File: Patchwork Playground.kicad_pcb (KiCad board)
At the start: 2 copper layers, 100 x 60 mm, 87 parts, among them J1 SWD_HEADER, J2 USB_C_Receptacle_USB2.0, J3 PADS, J4 POGO, J5 PADS, J6 JST-GH-4P, SW1 SW_SPDT, SW2 SW_SPDT, SW3 SW_SPDT, SW4 BUTTON, SW5 BUTTON, SW6 SW_SPDT, SW7 SW_SPDT, SW8 SW_SPDT, U1 SMF05CT1G, U2 M3406, U3 BQ21040DBVR, U4 SMF05CT1G, U5 QMC5883L, U6 BC805M, U7 LSM6DSV

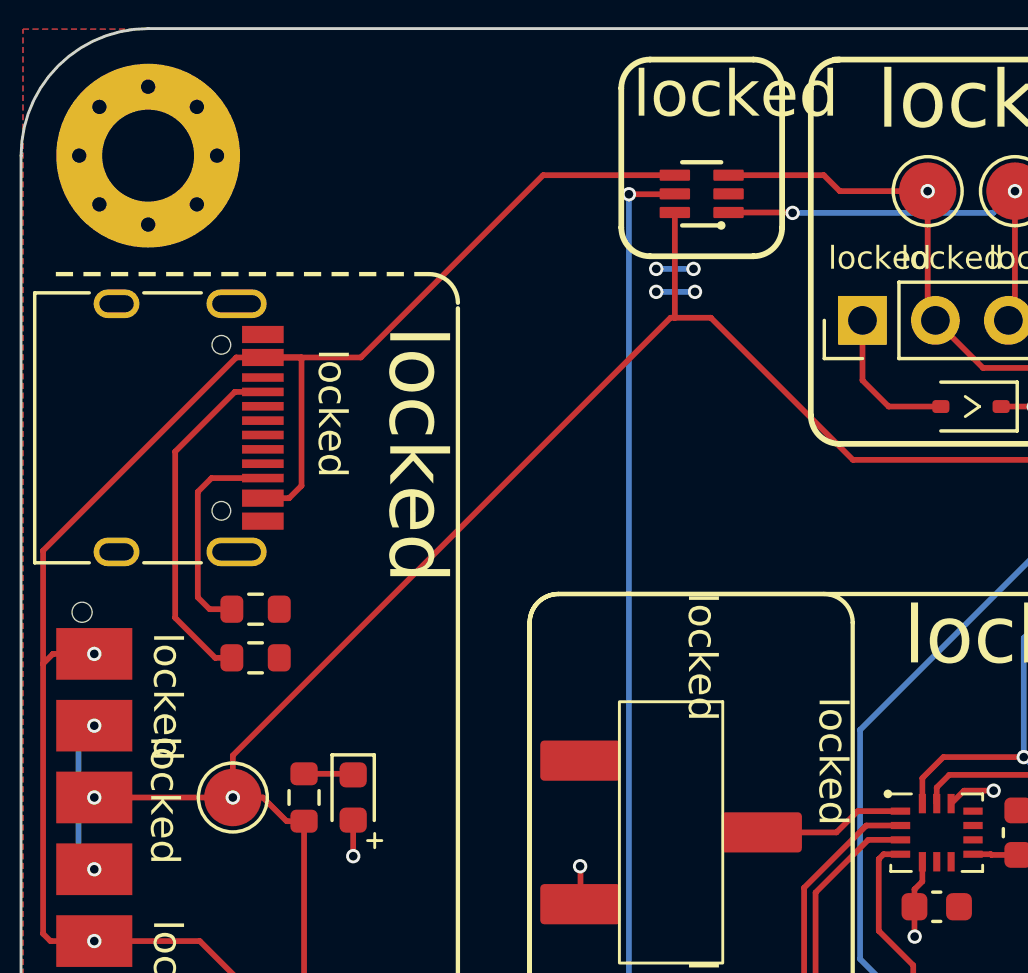
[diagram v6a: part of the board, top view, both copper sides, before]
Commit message: Minor routing changes
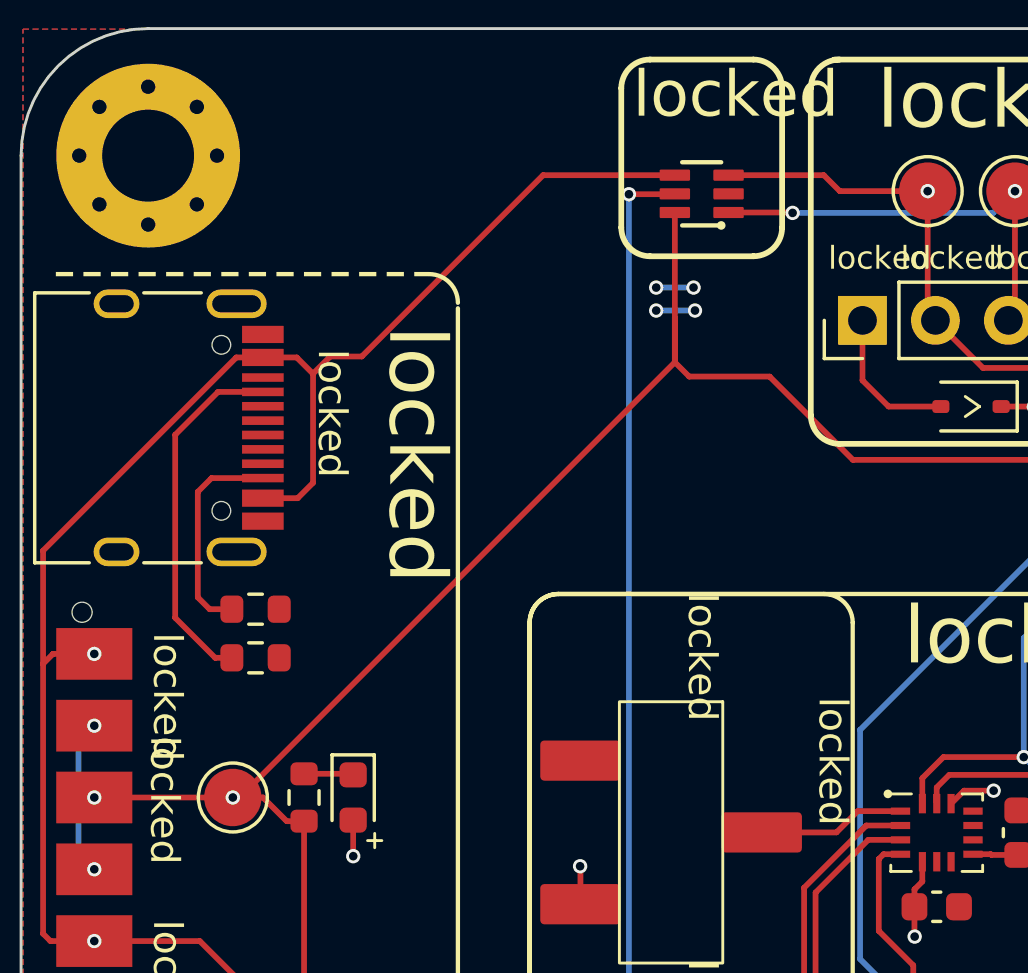
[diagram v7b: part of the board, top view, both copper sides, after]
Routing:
- net +5V: track 94.5 -> 93.4 mm
- net DOCK: track 84.6 -> 85.5 mm
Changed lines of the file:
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@@
   (via (at 100.4831 100.2565) (size 0.5) (drill 0.3) (layers "F.Cu" "B.Cu") (net 2))
   (via (at 114.4 126.1) (size 0.5) (drill 0.3) (layers "F.Cu" "B.Cu") (net 2))
-  (via (at 120.05 80.15) (size 0.5) (drill 0.3) (layers "F.Cu" "B.Cu") (free) (net 2))
-  (via (at 121.35 79.35) (size 0.5) (drill 0.3) (layers "F.Cu" "B.Cu") (free) (net 2))
-  (via (at 120.05 79.35) (size 0.5) (drill 0.3) (layers "F.Cu" "B.Cu") (free) (net 2))
+  (via (at 120.05 80.8) (size 0.5) (drill 0.3) (layers "F.Cu" "B.Cu") (free) (net 2))
+  (via (at 121.35 80) (size 0.5) (drill 0.3) (layers "F.Cu" "B.Cu") (free) (net 2))
+  (via (at 120.05 80) (size 0.5) (drill 0.3) (layers "F.Cu" "B.Cu") (free) (net 2))
   (via (at 100.4831 95.2565) (size 0.5) (drill 0.3) (layers "F.Cu" "B.Cu") (net 2))
-  (via (at 121.4 80.15) (size 0.5) (drill 0.3) (layers "F.Cu" "B.Cu") (free) (net 2))
+  (via (at 121.4 80.8) (size 0.5) (drill 0.3) (layers "F.Cu" "B.Cu") (free) (net 2))
   (segment (start 99.9331 95.8065) (end 100.4831 95.2565) (width 0.2) (layer "B.Cu") (net 2))
   (segment (start 100.4831 100.2565) (end 99.9331 99.7065) (width 0.2) (layer "B.Cu") (net 2))
-  (segment (start 121.35 79.35) (end 120.05 79.35) (width 0.2) (layer "B.Cu") (net 2))
-  (segment (start 120.05 80.15) (end 121.4 80.15) (width 0.2) (layer "B.Cu") (net 2))
+  (segment (start 121.35 80) (end 120.05 80) (width 0.2) (layer "B.Cu") (net 2))
+  (segment (start 120.05 80.8) (end 121.4 80.8) (width 0.2) (layer "B.Cu") (net 2))
   (segment (start 99.9331 99.7065) (end 99.9331 95.8065) (width 0.2) (layer "B.Cu") (net 2))
   (segment (start 119 126.1) (end 114.4 126.1) (width 0.2) (layer "B.Cu") (net 2))
@@
   (segment (start 171.4644 86.2144) (end 171.4644 86.8168) (width 0.2) (layer "F.Cu") (net 9))
   (segment (start 171.4394 86.1894) (end 171.4644 86.2144) (width 0.2) (layer "F.Cu") (net 9))
-  (segment (start 116.1132 76.0868) (end 120.699 76.0868) (width 0.2) (layer "F.Cu") (net 10))
   (segment (start 111.8 108.75) (end 129.0069 125.9569) (width 0.2) (layer "F.Cu") (net 10))
-  (segment (start 107.7 82.434) (end 106.3531 82.434) (width 0.2) (layer "F.Cu") (net 10))
   (segment (start 109.3 108.75) (end 111.8 108.75) (width 0.2) (layer "F.Cu") (net 10))
   (segment (start 98.7 93.1) (end 98.7 89.1621) (width 0.2) (layer "F.Cu") (net 10))
-  (segment (start 106.3531 82.434) (end 109.766 82.434) (width 0.2) (layer "F.Cu") (net 10))
+  (segment (start 116.1132 76.0868) (end 109.8 82.4) (width 0.2) (layer "F.Cu") (net 10))
+  (segment (start 107.566 87.334) (end 108.1 86.8) (width 0.2) (layer "F.Cu") (net 10))
   (segment (start 100.4831 92.7565) (end 99.0435 92.7565) (width 0.2) (layer "F.Cu") (net 10))
   (segment (start 99.0435 92.7565) (end 98.7 93.1) (width 0.2) (layer "F.Cu") (net 10))
+  (segment (start 106.3531 87.334) (end 107.566 87.334) (width 0.2) (layer "F.Cu") (net 10))
   (segment (start 106.0081 104.6081) (end 106.0081 106.559) (width 0.2) (layer "F.Cu") (net 10))
+  (segment (start 108.7 82.4) (end 108.1 83) (width 0.2) (layer "F.Cu") (net 10))
+  (segment (start 120.699 76.0868) (end 116.1132 76.0868) (width 0.2) (layer "F.Cu") (net 10))
   (segment (start 98.7 102.5) (end 98.7 93.1) (width 0.2) (layer "F.Cu") (net 10))
   (segment (start 104.1565 102.7565) (end 106.0081 104.6081) (width 0.2) (layer "F.Cu") (net 10))
-  (segment (start 107.266 87.334) (end 107.7 86.9) (width 0.2) (layer "F.Cu") (net 10))
+  (segment (start 107.534 82.434) (end 106.3531 82.434) (width 0.2) (layer "F.Cu") (net 10))
   (segment (start 106.0081 106.559) (end 106.991 106.559) (width 0.2) (layer "F.Cu") (net 10))
-  (segment (start 107.7 86.9) (end 107.7 82.434) (width 0.2) (layer "F.Cu") (net 10))
   (segment (start 98.7 89.1621) (end 105.4281 82.434) (width 0.2) (layer "F.Cu") (net 10))
-  (segment (start 109.766 82.434) (end 116.1132 76.0868) (width 0.2) (layer "F.Cu") (net 10))
   (segment (start 100.4831 102.7565) (end 104.1565 102.7565) (width 0.2) (layer "F.Cu") (net 10))
   (segment (start 106.991 106.559) (end 107.05 106.5) (width 0.2) (layer "F.Cu") (net 10))
@@
   (segment (start 100.4831 102.7565) (end 98.9565 102.7565) (width 0.2) (layer "F.Cu") (net 10))
   (segment (start 129.0069 125.9569) (end 132.2884 125.9569) (width 0.2) (layer "F.Cu") (net 10))
-  (segment (start 106.3531 87.334) (end 107.266 87.334) (width 0.2) (layer "F.Cu") (net 10))
+  (segment (start 109.8 82.4) (end 108.7 82.4) (width 0.2) (layer "F.Cu") (net 10))
+  (segment (start 108.1 86.8) (end 108.1 83) (width 0.2) (layer "F.Cu") (net 10))
+  (segment (start 108.1 83) (end 107.534 82.434) (width 0.2) (layer "F.Cu") (net 10))
   (via (at 107.05 106.5) (size 0.5) (drill 0.3) (layers "F.Cu" "B.Cu") (net 10))
   (via (at 100.4831 92.7565) (size 0.5) (drill 0.3) (layers "F.Cu" "B.Cu") (net 10))
@@
   (segment (start 131.7857 77.4) (end 132.5431 76.6426) (width 0.2) (layer "B.Cu") (net 27))
   (segment (start 124.8 77.4) (end 131.7857 77.4) (width 0.2) (layer "B.Cu") (net 27))
+  (segment (start 103.3 85.127786) (end 104.793786 83.634) (width 0.2) (layer "F.Cu") (net 28))
+  (segment (start 103.3 91.5) (end 103.3 85.127786) (width 0.2) (layer "F.Cu") (net 28))
+  (segment (start 104.793786 83.634) (end 106.3531 83.634) (width 0.2) (layer "F.Cu") (net 28))
   (segment (start 105.2731 92.8935) (end 104.6935 92.8935) (width 0.2) (layer "F.Cu") (net 28))
-  (segment (start 103.3 85.7121) (end 105.3781 83.634) (width 0.2) (layer "F.Cu") (net 28))
   (segment (start 104.6935 92.8935) (end 103.3 91.5) (width 0.2) (layer "F.Cu") (net 28))
-  (segment (start 103.3 91.5) (end 103.3 85.7121) (width 0.2) (layer "F.Cu") (net 28))
-  (segment (start 105.3781 83.634) (end 106.3531 83.634) (width 0.2) (layer "F.Cu") (net 28))
   (segment (start 105.2731 91.2) (end 104.5 91.2) (width 0.2) (layer "F.Cu") (net 32))
   (segment (start 104.5 91.2) (end 104.0881 90.7881) (width 0.2) (layer "F.Cu") (net 32))
@@
   (segment (start 104.0881 90.7881) (end 104.0881 87.1119) (width 0.2) (layer "F.Cu") (net 32))
   (segment (start 104.0881 87.1119) (end 104.566 86.634) (width 0.2) (layer "F.Cu") (net 32))
+  (segment (start 120.699 82.599) (end 121.2 83.1) (width 0.2) (layer "F.Cu") (net 36))
   (segment (start 107.7876 111.7124) (end 105.4034 114.0966) (width 0.2) (layer "F.Cu") (net 36))
-  (segment (start 120.549 81.051) (end 120.699 81.051) (width 0.2) (layer "F.Cu") (net 36))
+  (segment (start 105.3081 97.7565) (end 105.5435 97.7565) (width 0.2) (layer "F.Cu") (net 36))
+  (segment (start 124 83.1) (end 126.9 86) (width 0.2) (layer "F.Cu") (net 36))
   (segment (start 105.3081 97.7565) (end 100.4831 97.7565) (width 0.2) (layer "F.Cu") (net 36))
+  (segment (start 120.699 81.051) (end 120.699 82.599) (width 0.2) (layer "F.Cu") (net 36))
+  (segment (start 105.5435 97.7565) (end 120.699 82.601) (width 0.2) (layer "F.Cu") (net 36))
+  (segment (start 105.4034 114.0966) (end 104.1831 114.0966) (width 0.2) (layer "F.Cu") (net 36))
   (segment (start 139.1731 81.1269) (end 143.0081 81.1269) (width 0.2) (layer "F.Cu") (net 36))
-  (segment (start 105.4034 114.0966) (end 104.1831 114.0966) (width 0.2) (layer "F.Cu") (net 36))
   (segment (start 104.1831 120.0966) (end 104.1831 114.0966) (width 0.2) (layer "F.Cu") (net 36))
   (segment (start 106.3565 97.7565) (end 107.1815 98.5815) (width 0.2) (layer "F.Cu") (net 36))
-  (segment (start 105.3081 96.2919) (end 120.549 81.051) (width 0.2) (layer "F.Cu") (net 36))
-  (segment (start 120.699 81.051) (end 121.951 81.051) (width 0.2) (layer "F.Cu") (net 36))
+  (segment (start 134.3 86) (end 139.1731 81.1269) (width 0.2) (layer "F.Cu") (net 36))
   (segment (start 120.699 81.051) (end 120.699 77.3868) (width 0.2) (layer "F.Cu") (net 36))
+  (segment (start 107.1815 98.5815) (end 107.7876 98.5815) (width 0.2) (layer "F.Cu") (net 36))
   (segment (start 126.9 86) (end 134.3 86) (width 0.2) (layer "F.Cu") (net 36))
-  (segment (start 107.1815 98.5815) (end 107.7876 98.5815) (width 0.2) (layer "F.Cu") (net 36))
-  (segment (start 121.951 81.051) (end 126.9 86) (width 0.2) (layer "F.Cu") (net 36))
+  (segment (start 120.699 82.601) (end 120.699 81.051) (width 0.2) (layer "F.Cu") (net 36))
   (segment (start 105.3081 97.7565) (end 106.3565 97.7565) (width 0.2) (layer "F.Cu") (net 36))
-  (segment (start 134.3 86) (end 139.1731 81.1269) (width 0.2) (layer "F.Cu") (net 36))
   (segment (start 107.7876 98.5815) (end 107.7876 111.7124) (width 0.2) (layer "F.Cu") (net 36))
-  (segment (start 105.3081 97.7565) (end 105.3081 96.2919) (width 0.2) (layer "F.Cu") (net 36))
+  (segment (start 121.2 83.1) (end 124 83.1) (width 0.2) (layer "F.Cu") (net 36))
   (via (at 105.3081 97.7565) (size 0.5) (drill 0.3) (layers "F.Cu" "B.Cu") (net 36))
   (via (at 100.4831 97.7565) (size 0.5) (drill 0.3) (layers "F.Cu" "B.Cu") (net 36))
